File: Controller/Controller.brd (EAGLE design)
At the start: 36.3 x 29.8 mm, 43 parts, among them SW1 SWITCH-PTS-810, U1 ATSAMD21E18A-AU, U2 MIC5205-3.3YM5 TR, X1 CRYSTAL-AB26TRQ-32.768K

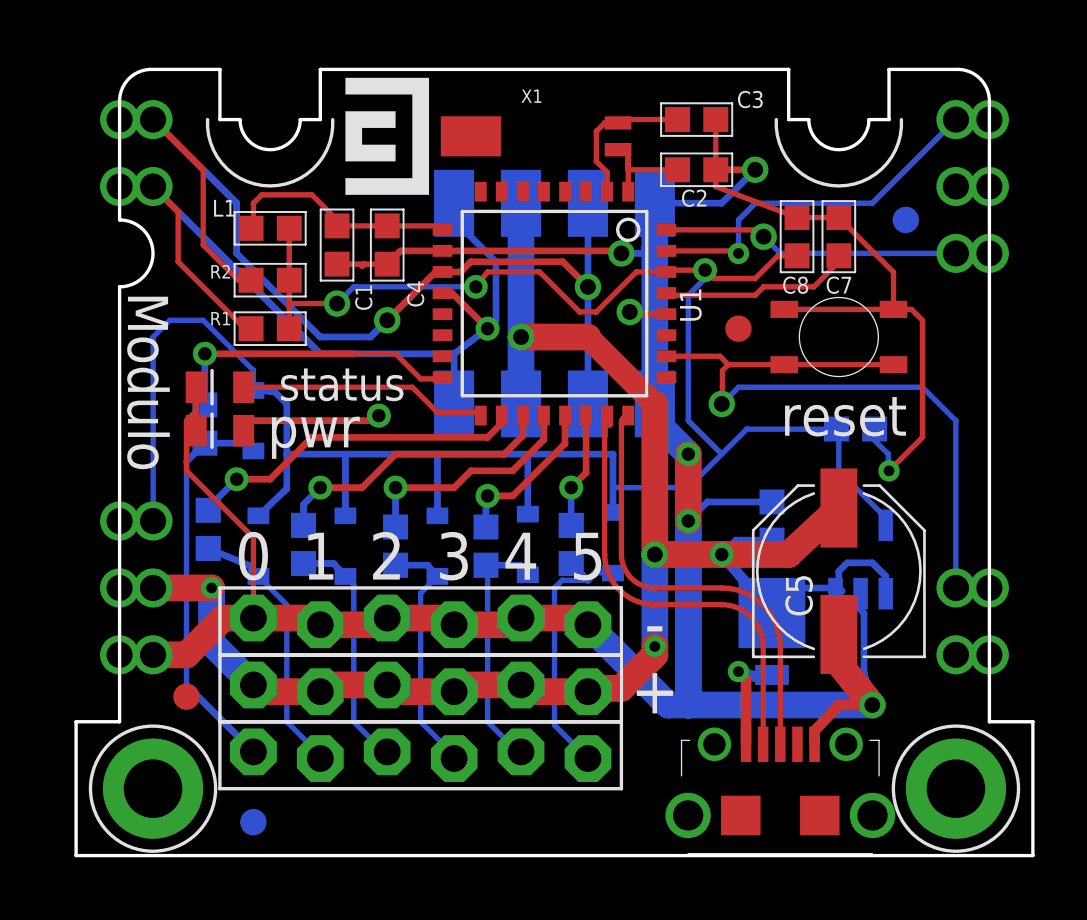
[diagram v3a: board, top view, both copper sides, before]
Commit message: Fixed bad clamp diode wiring and added a reverse protection diode
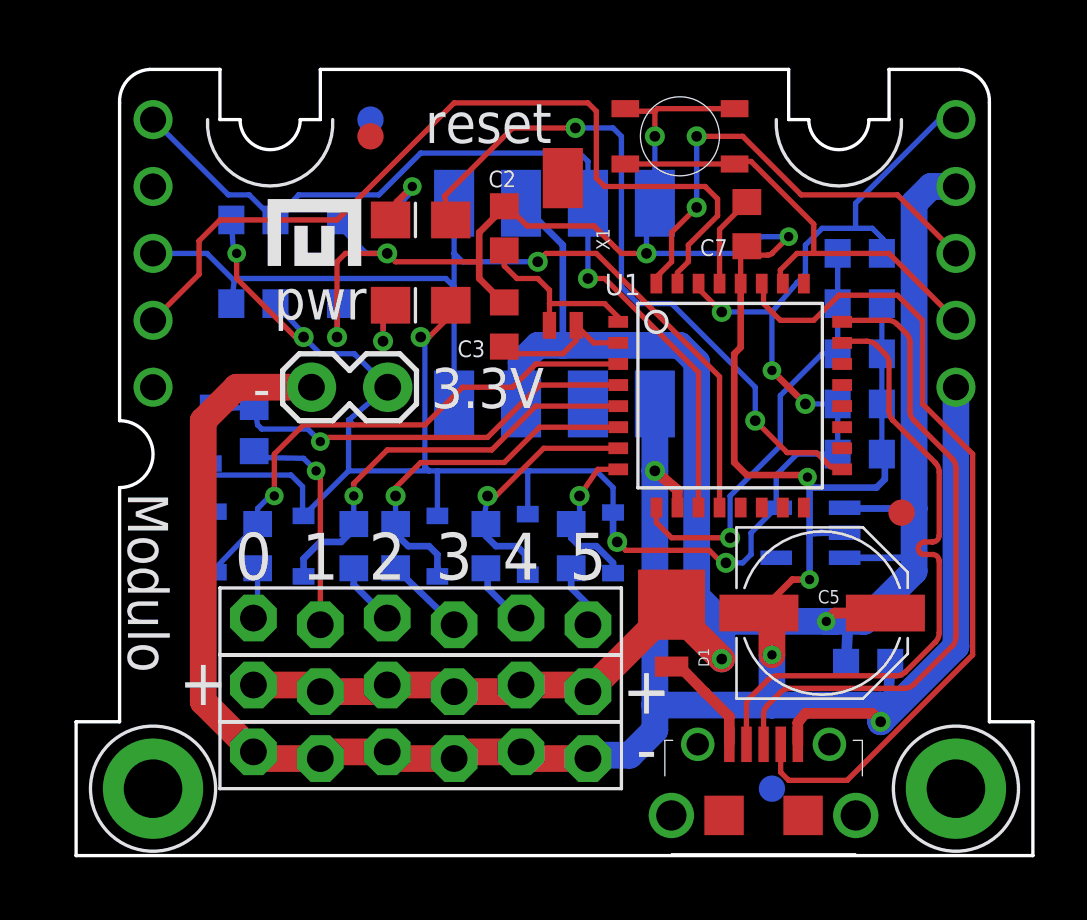
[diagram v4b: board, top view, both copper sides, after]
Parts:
- removed U$1: (no value), Modulo:LOGO-SMALL
- added JP6: M02LOCK, SparkFun-Connectors:1X02_LOCK
- added R10, R9: 1KΩ, Modulo:0603
- U$2: device Modulo:LOGO-SMALL -> Modulo:LOGO-TINY
- moved L1 22.4 mm to (29.4, 22.9), flipped to the bottom, turned to 0 degrees
- moved F1 22.4 mm to (10.8, 27.3)
- moved F3 20.7 mm to (10.8, 27.9)
- moved C1 20.3 mm to (29.4, 19.1), flipped to the bottom, turned to 180 degrees
- moved F4 19.7 mm to (26.0, 2.54)
- moved C4 18.1 mm to (29.4, 21.0), flipped to the bottom, turned to 180 degrees
- moved C3 10.7 mm to (15.9, 20.2), turned to 270 degrees
- moved LED2 9.92 mm to (12.7, 24.1)
- moved SW1 9.72 mm to (22.5, 27.3)
- moved F2 9.33 mm to (31.0, 13.0)
- moved LED1 8.99 mm to (12.7, 20.9)
- moved C8 8.59 mm to (29.4, 15.2), flipped to the bottom, turned to 180 degrees
- moved C2 7.63 mm to (15.9, 23.8), turned to 270 degrees
- moved U1 7.53 mm to (24.4, 17.5), turned to 0 degrees
- moved C6 6.52 mm to (29.7, 7.30), turned to 180 degrees
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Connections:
- new net N$1: LED1.C, R9.2
- new net N$4: LED2.C, R10.2
- new net N_HOST_ENABLE: JP1.P4, U1.27
- net +3.3V: now also JP6.1
- net GND: now also JP6.2, R10.1, R9.1; no longer LED1.C, LED2.C
- net IO0: now also D7.A, U1.3; no longer U1.16
- net IO1: now also D6.A, U1.4; no longer U1.18
- net IO2: now also D5.A, U1.5; no longer U1.19
- net IO3: now also D4.A, U1.6; no longer U1.20
- net IO4: now also D3.A, U1.7; no longer U1.21
- net IO5: now also D2.A, U1.8; no longer U1.22
- net N$13: no longer D3.A
- net N$17: no longer D4.A
- net N$18: no longer D5.A
- net N$19: no longer D6.A
- net N$2: no longer D2.A
- net N$20: no longer D7.A
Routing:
- net GND: track 120.9 -> 153.4 mm, vias 7 -> 10
- net N_HOST_ENABLE: track 0.00 -> 31.8 mm
- net SWCLK: track 13.9 -> 32.4 mm, vias 1 -> 0
- net LED: track 9.45 -> 26.5 mm, vias 0 -> 2
- net VCC: track 66.5 -> 82.2 mm, vias 5 -> 2
- net N$20: track 15.0 -> 1.96 mm
- net +3.3V: track 96.4 -> 83.6 mm, vias 4 -> 8
- net IO0: track 11.4 -> 19.9 mm
- net RESET: track 26.4 -> 18.2 mm, vias 1 -> 0
- net N$2: track 10.4 -> 2.41 mm
- net D+: track 16.7 -> 24.6 mm
- net N$21: track 8.98 -> 16.4 mm, vias 0 -> 1
- net D-: track 17.0 -> 24.3 mm
- net N$13: track 9.79 -> 2.57 mm
- net N$18: track 9.20 -> 2.42 mm
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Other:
- outline, holes or cut-outs redrawn
- board text added: "3.3V"
- board text removed: "status"

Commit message: Various small tweaks based on testing and feedback from manufacturer.
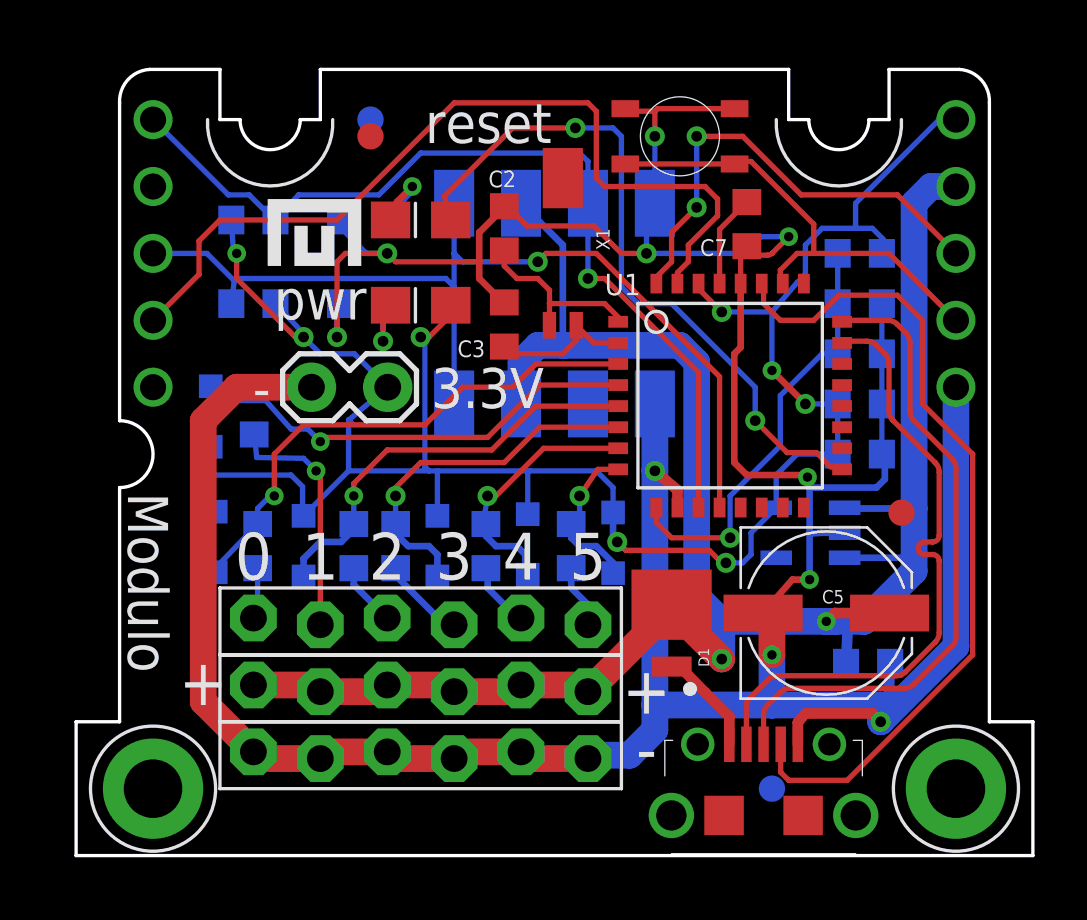
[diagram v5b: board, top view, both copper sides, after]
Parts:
- R1, R2: value 1KΩ -> 5kΩ
- U2: value MIC5205-3.3YM5 TR -> VREG-MIC5205-3.3V
- moved R7 0.64 mm to (6.38, 16.8)
- moved D6 0.63 mm to (4.73, 16.7)
- moved C5 0.16 mm to (28.1, 9.21)
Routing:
- net IO1: track 17.3 -> 18.0 mm
- net +3.3V: track 83.6 -> 84.2 mm
- net N$19: track 8.62 -> 9.24 mm

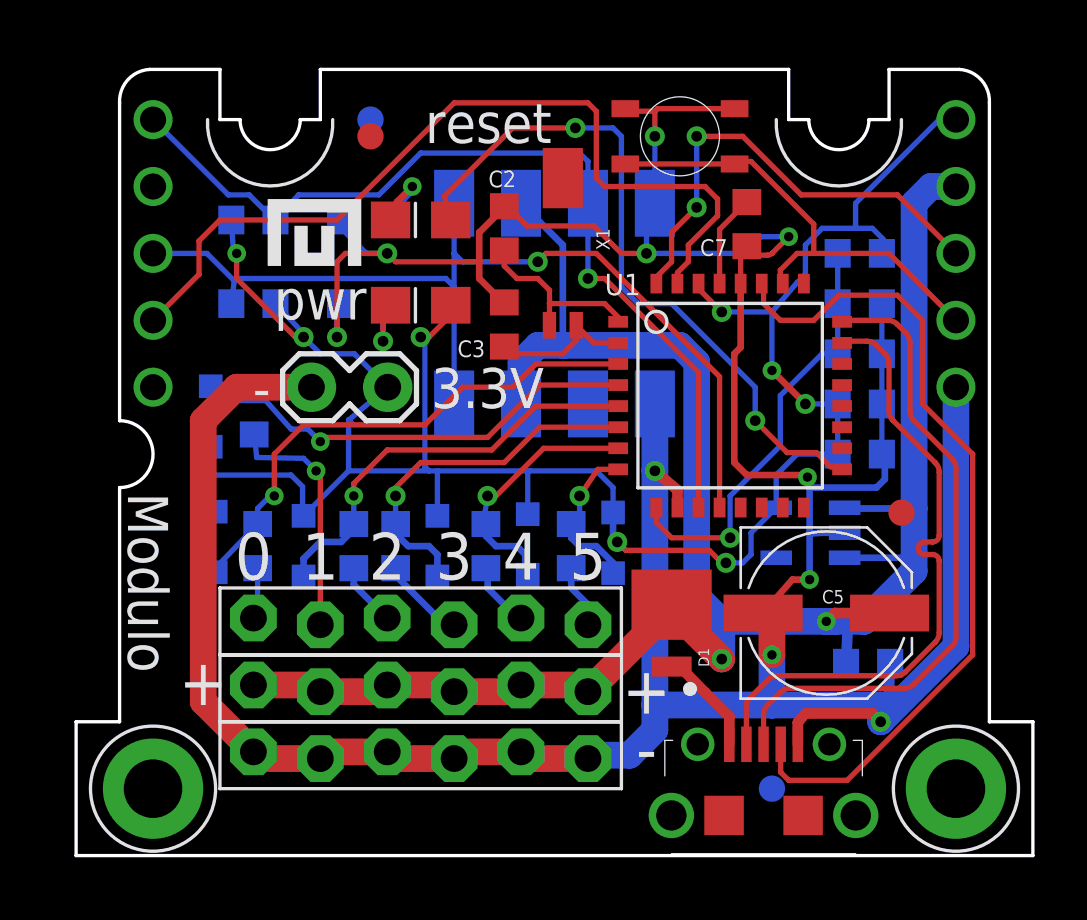
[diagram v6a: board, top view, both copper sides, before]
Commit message: Added unique board prefixes to part numbers due to CM requirements
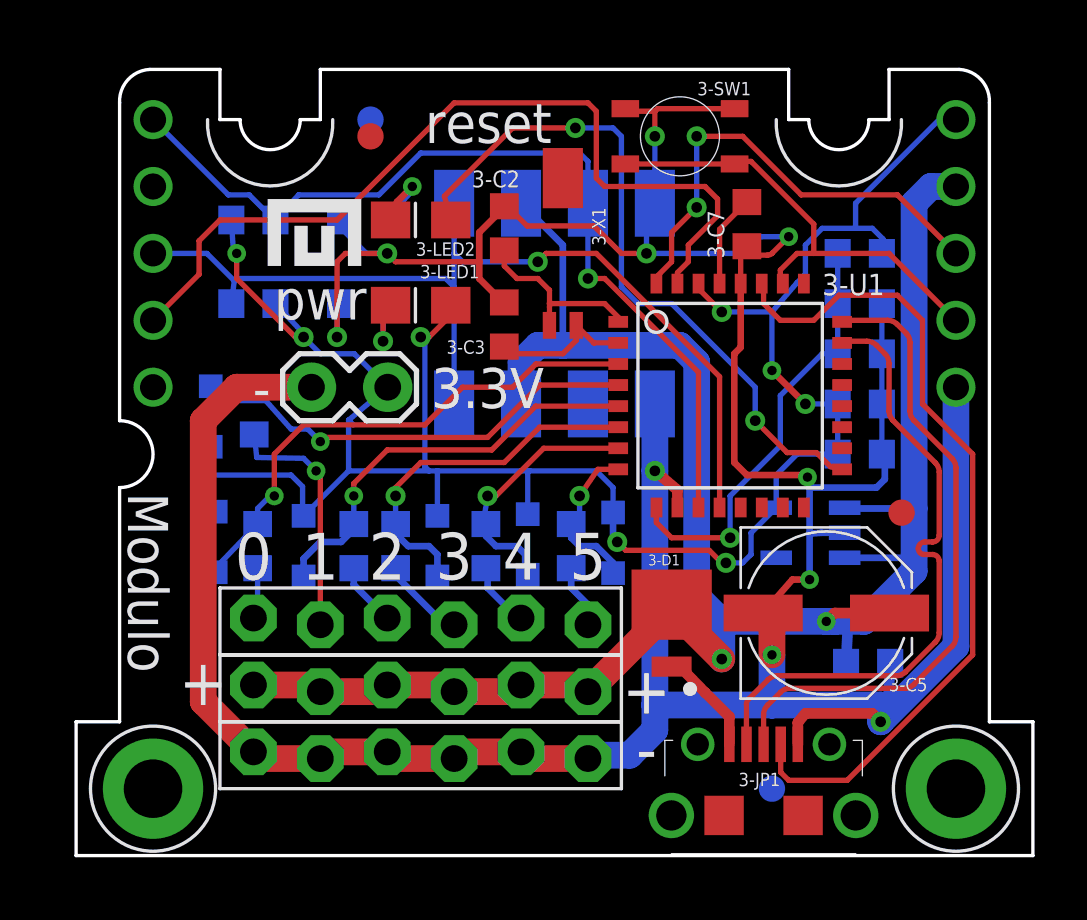
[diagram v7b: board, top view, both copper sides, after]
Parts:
- renumbered C1 to 3-C1, C2 to 3-C2, C3 to 3-C3, C4 to 3-C4, C5 to 3-C5, C6 to 3-C6, C7 to 3-C7, C8 to 3-C8, C9 to 3-C9, D1 to 3-D1, D2 to 3-D2, D3 to 3-D3, D4 to 3-D4, D5 to 3-D5, D6 to 3-D6, D7 to 3-D7, JP1 to 3-JP1, JP2 to 3-JP2, JP3 to 3-JP3, JP4 to 3-JP4, JP5 to 3-JP5, JP6 to 3-JP6, L1 to 3-L1, LED1 to 3-LED1, LED2 to 3-LED2, PCB1 to 3-PCB1, R1 to 3-R1, R10 to 3-R10, R2 to 3-R2, R3 to 3-R3, R4 to 3-R4, R5 to 3-R5, R6 to 3-R6, R7 to 3-R7, R8 to 3-R8, R9 to 3-R9, SW1 to 3-SW1, U1 to 3-U1, U2 to 3-U2, X1 to 3-X1
